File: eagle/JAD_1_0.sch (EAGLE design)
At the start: 16 parts, among them X1 A1, X2 A2, X3 A3, X4 B1, X5 B2, X6 B3

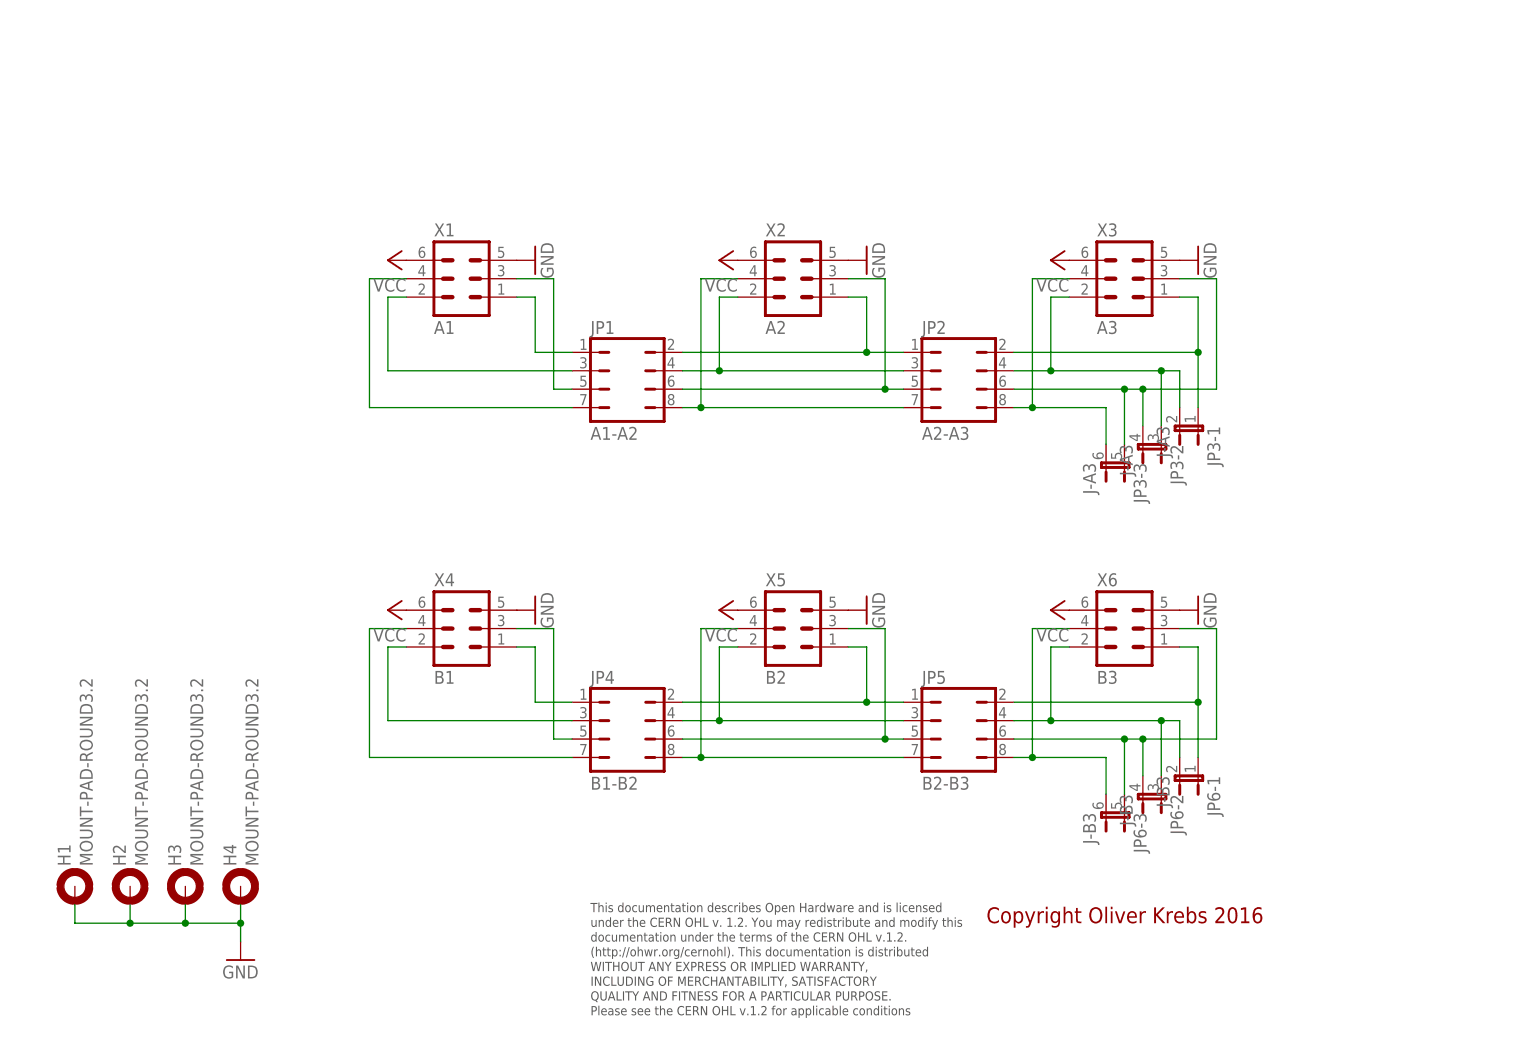
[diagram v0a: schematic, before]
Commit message: Add new tetra-Board and arduino files
Add AMP_1_0, AVC_1_0, D18_1_1, IOP_1_2, MIC_1_0, PIN_1_1, POT_1_0, PWA_1_0, PWR_1_0, RGF 2.0, SOC_2_0, VLT_1_0
Add mex_nano_shield_keyboard, mex_nano_shied_numbers

New arduino projects
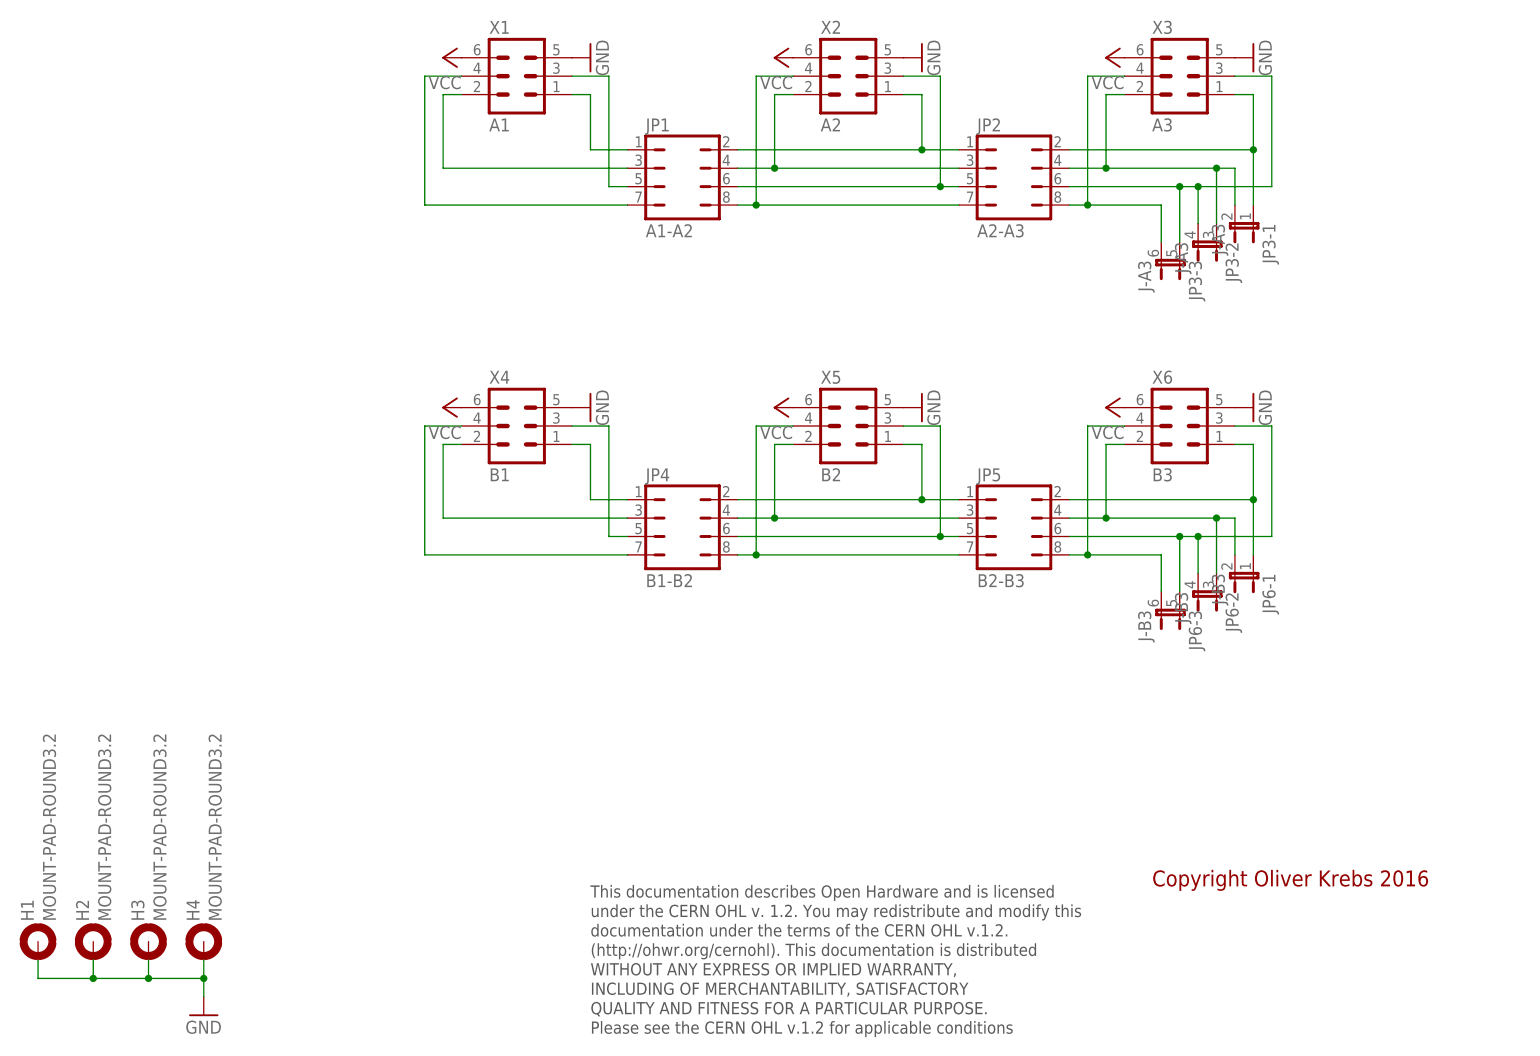
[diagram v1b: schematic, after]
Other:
- moved on the sheet: H1, H2, H3, H4, JP1, JP2, JP3-1, JP3-2, JP3-3, JP4, JP5, JP6-1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
